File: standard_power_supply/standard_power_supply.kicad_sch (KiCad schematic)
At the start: 7 parts, among them J1 220V, J4 +35V 0 -35V, T1 25 - 0 - 25

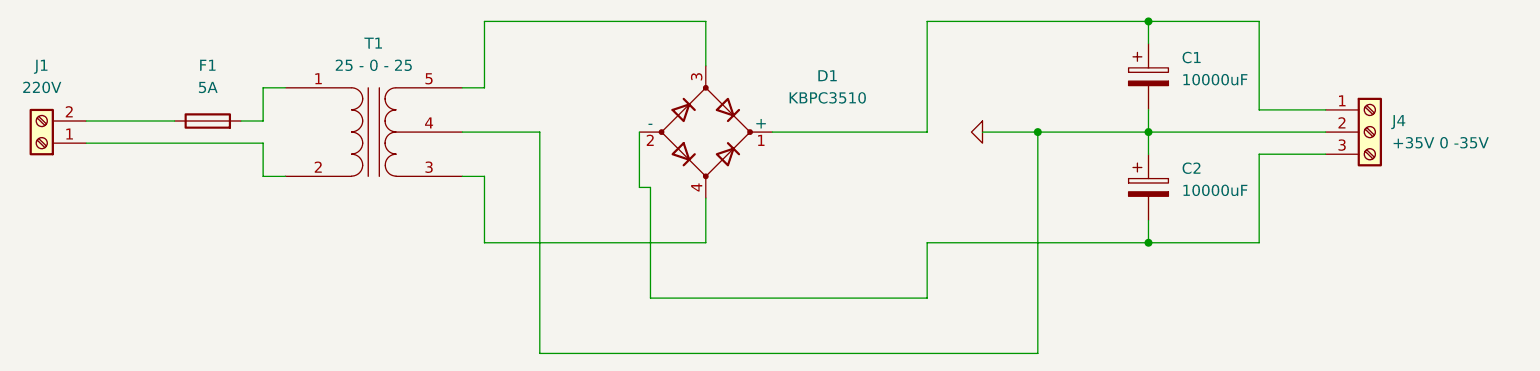
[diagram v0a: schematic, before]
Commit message: 40V upgrade and generate BOM CSVs
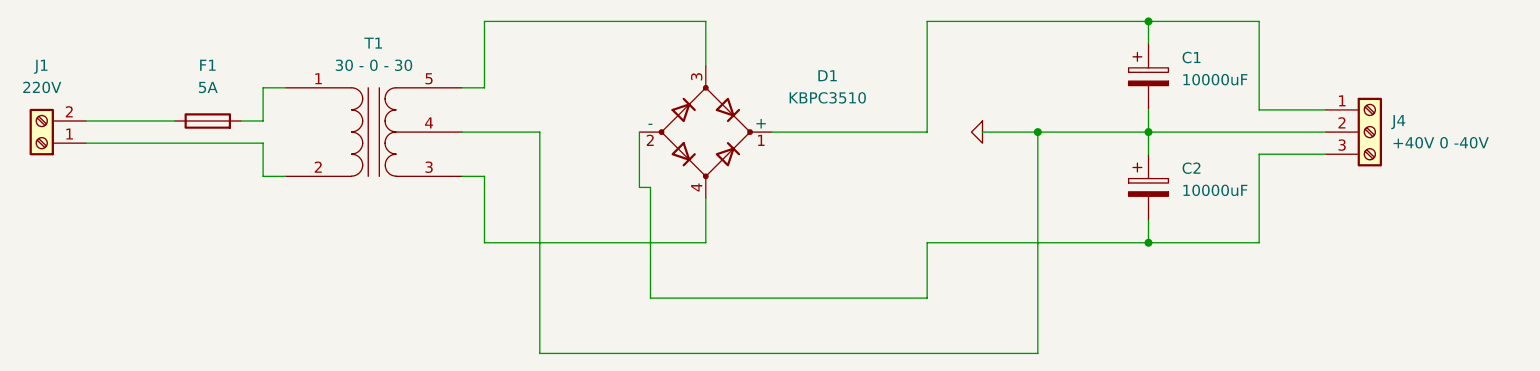
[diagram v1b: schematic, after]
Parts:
- J4: value +35V 0 -35V -> +40V 0 -40V
- T1: value 25 - 0 - 25 -> 30 - 0 - 30
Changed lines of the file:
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@@
 			)
 		)
-		(property "Value" "+35V 0 -35V"
+		(property "Value" "+40V 0 -40V"
 			(at 205.74 64.7699 0)
 			(effects
@@
 			)
 		)
-		(property "Value" "25 - 0 - 25"
+		(property "Value" "30 - 0 - 30"
 			(at 88.9127 55.88 0)
 			(effects

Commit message: Finished PSU PCB Design
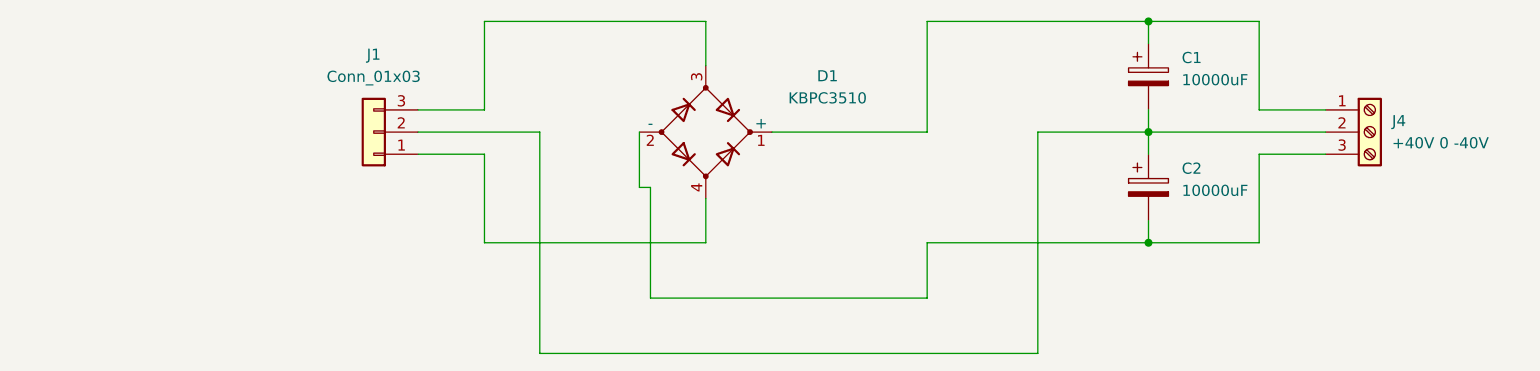
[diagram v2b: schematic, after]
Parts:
- removed F1: 5A, symbol Device:Fuse
- removed J1: 220V, symbol Connector:Screw_Terminal_01x02
- removed T1: 30 - 0 - 30, symbol Device:Transformer_1P_SS
- added J1: Conn_01x03, TerminalBlock_Phoenix:TerminalBlock_Phoenix_MKDS-1,5-3-5.08_1x03_P5.08mm_Horizontal, symbol Connector_Generic:Conn_01x03
- C1, C2: footprint (none) -> Capacitor_THT:CP_Radial_D35.0mm_P10.00mm_SnapIn
- D1: footprint (none) -> Diode_THT:Diode_Bridge_28.6x28.6x7.3mm_P18.0mm_P11.6mm
- J4: footprint (none) -> TerminalBlock_Phoenix:TerminalBlock_Phoenix_MKDS-1,5-3-5.08_1x03_P5.08mm_Horizontal
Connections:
- net at D1.3: now also J1.3 (Pin_3)
- net at D1.4: now also J1.1 (Pin_1)
- net 0: no longer names the net of C1.2, C2.1, J4.2 (Pin_2)
- net 0: now also J1.2 (Pin_2)
